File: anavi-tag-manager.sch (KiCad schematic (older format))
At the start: 26 parts, among them J1 USB_B_Micro, P1 CONN_01X03, SW1 SW_DIP_x01, U1 I2C_SENS_1, U2 I2C_SENS_1, U3 I2C_SENS_1, U4 Conn_01x04, U5 Conn_01x04, U6 Conn_01x04

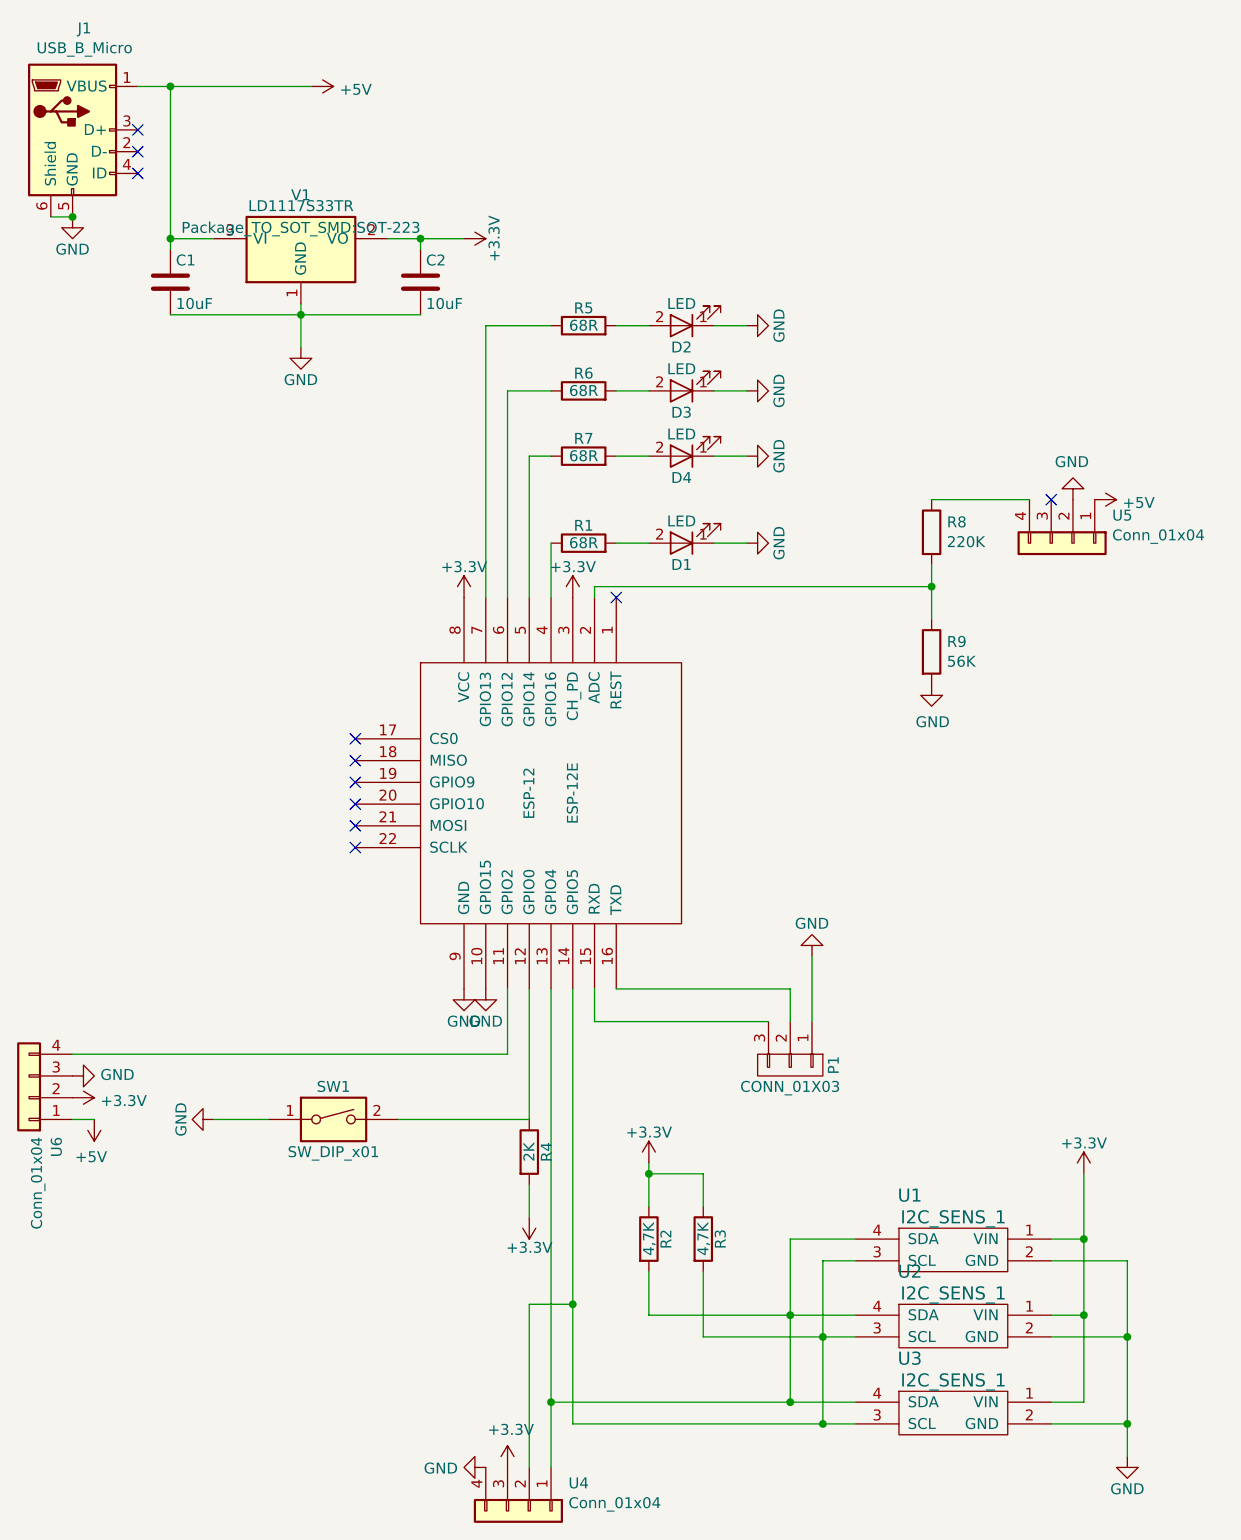
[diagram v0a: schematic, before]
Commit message: anavi-tag-manager.sch: Modify schematics
Remove unnecessary components inherited by ANAVI Gas Detector.
Add 4.7K resistor to GPIO15 of ESP8266. This way it is possible
to use this pin for SPI communicaiton after booting the board:
https://github.com/esp8266/Arduino/issues/2466#issuecomment-330794960

Signed-off-by: Leon Anavi <leon@anavi.org>
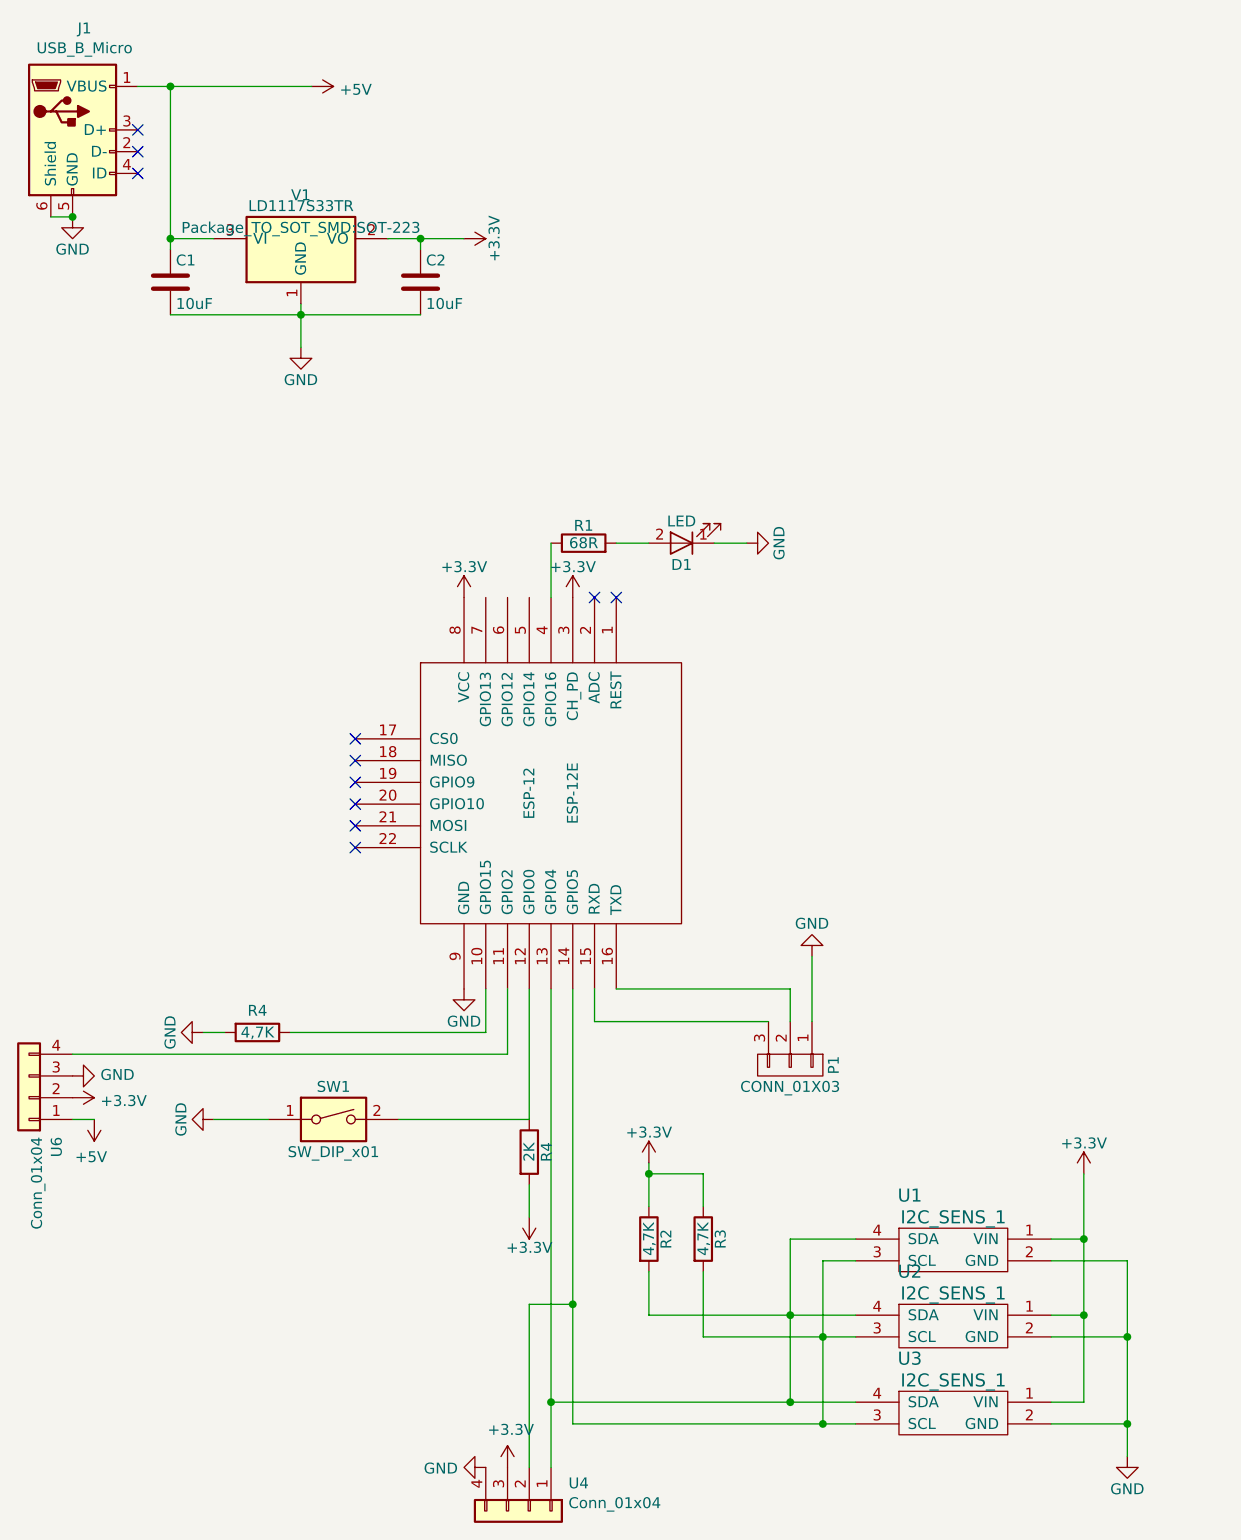
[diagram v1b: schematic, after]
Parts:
- removed D2, D3, D4: LED, LED_SMD:LED_1206_3216Metric, symbol anavi-tag-manager-rescue:LED-anavi-thermometer-rescue-anavi-gas-detector-rescue
- removed R5, R6, R7: 68R, Resistor_SMD:R_0603_1608Metric, symbol anavi-tag-manager-rescue:R-anavi-thermometer-rescue-anavi-gas-detector-rescue
- removed R8: 220K, Resistor_SMD:R_0603_1608Metric, symbol Device:R
- removed R9: 56K, Resistor_SMD:R_0603_1608Metric, symbol Device:R
- removed U5: Conn_01x04, Connector_PinHeader_2.54mm:PinHeader_1x04_P2.54mm_Vertical, symbol Connector_Generic:Conn_01x04
- added R4: 4,7K, Resistor_SMD:R_0603_1608Metric, symbol anavi-tag-manager-rescue:R-anavi-thermometer-rescue-anavi-gas-detector-rescue
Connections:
- net GND: now also R4.2; no longer ESP-12.10 (GPIO15)
- new net: ESP-12.10 (GPIO15), R4.1
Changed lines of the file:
@@
 L anavi-tag-manager-rescue:GND-anavi-thermometer-rescue-anavi-gas-detector-rescue #PWR018
 U 1 1 59B811E0
-P 2850 5100
-F 0 "#PWR018" H 2850 4850 50  0001 C CNN
-F 1 "GND" H 2850 4950 50  0000 C CNN
-F 2 "" H 2850 5100 50  0000 C CNN
-F 3 "" H 2850 5100 50  0000 C CNN
-	1    2850 5100
-	1    0    0    -1
+P 1550 5300
+F 0 "#PWR018" H 1550 5050 50  0001 C CNN
+F 1 "GND" H 1550 5150 50  0000 C CNN
+F 2 "" H 1550 5300 50  0000 C CNN
+F 3 "" H 1550 5300 50  0000 C CNN
+	1    1550 5300
+	0    1    1    0
 $EndComp
 $Comp
@@
 $EndComp
 $Comp
-L anavi-tag-manager-rescue:LED-anavi-thermometer-rescue-anavi-gas-detector-rescue D4
-U 1 1 5CAADB24
-P 3750 2650
-F 0 "D4" H 3750 2750 50  0000 C CNN
-F 1 "LED" H 3750 2550 50  0000 C CNN
-F 2 "LED_SMD:LED_1206_3216Metric" H 3750 2650 50  0001 C CNN
-F 3 "" H 3750 2650 50  0000 C CNN
-	1    3750 2650
-	-1   0    0    1
-$EndComp
-$Comp
-L anavi-tag-manager-rescue:R-anavi-thermometer-rescue-anavi-gas-detector-rescue R7
-U 1 1 5CAADB2B
-P 3300 2650
-F 0 "R7" V 3380 2650 50  0000 C CNN
-F 1 "68R" V 3300 2650 50  0000 C CNN
-F 2 "Resistor_SMD:R_0603_1608Metric" V 3230 2650 50  0001 C CNN
-F 3 "" H 3300 2650 50  0000 C CNN
-	1    3300 2650
-	0    -1   -1   0
-$EndComp
-$Comp
-L anavi-tag-manager-rescue:GND-anavi-thermometer-rescue-anavi-gas-detector-rescue #PWR?
-U 1 1 5CAADB32
-P 4050 2650
-F 0 "#PWR?" H 4050 2400 50  0001 C CNN
-F 1 "GND" H 4050 2500 50  0000 C CNN
-F 2 "" H 4050 2650 50  0000 C CNN
-F 3 "" H 4050 2650 50  0000 C CNN
-	1    4050 2650
-	0    -1   -1   0
-$EndComp
-Wire Wire Line
-	3450 2650 3600 2650
-Wire Wire Line
-	3900 2650 4050 2650
-$Comp
-L anavi-tag-manager-rescue:LED-anavi-thermometer-rescue-anavi-gas-detector-rescue D3
-U 1 1 5CAAEF49
-P 3750 2350
-F 0 "D3" H 3750 2450 50  0000 C CNN
-F 1 "LED" H 3750 2250 50  0000 C CNN
-F 2 "LED_SMD:LED_1206_3216Metric" H 3750 2350 50  0001 C CNN
-F 3 "" H 3750 2350 50  0000 C CNN
-	1    3750 2350
-	-1   0    0    1
-$EndComp
-$Comp
-L anavi-tag-manager-rescue:R-anavi-thermometer-rescue-anavi-gas-detector-rescue R6
-U 1 1 5CAAEF50
-P 3300 2350
-F 0 "R6" V 3380 2350 50  0000 C CNN
-F 1 "68R" V 3300 2350 50  0000 C CNN
-F 2 "Resistor_SMD:R_0603_1608Metric" V 3230 2350 50  0001 C CNN
-F 3 "" H 3300 2350 50  0000 C CNN
-	1    3300 2350
-	0    -1   -1   0
-$EndComp
-$Comp
-L anavi-tag-manager-rescue:GND-anavi-thermometer-rescue-anavi-gas-detector-rescue #PWR?
-U 1 1 5CAAEF57
-P 4050 2350
-F 0 "#PWR?" H 4050 2100 50  0001 C CNN
-F 1 "GND" H 4050 2200 50  0000 C CNN
-F 2 "" H 4050 2350 50  0000 C CNN
-F 3 "" H 4050 2350 50  0000 C CNN
-	1    4050 2350
-	0    -1   -1   0
-$EndComp
-Wire Wire Line
-	3450 2350 3600 2350
-Wire Wire Line
-	3900 2350 4050 2350
-$Comp
-L anavi-tag-manager-rescue:LED-anavi-thermometer-rescue-anavi-gas-detector-rescue D2
-U 1 1 5CAB04B0
-P 3750 2050
-F 0 "D2" H 3750 2150 50  0000 C CNN
-F 1 "LED" H 3750 1950 50  0000 C CNN
-F 2 "LED_SMD:LED_1206_3216Metric" H 3750 2050 50  0001 C CNN
-F 3 "" H 3750 2050 50  0000 C CNN
-	1    3750 2050
-	-1   0    0    1
-$EndComp
-$Comp
-L anavi-tag-manager-rescue:R-anavi-thermometer-rescue-anavi-gas-detector-rescue R5
-U 1 1 5CAB04B7
-P 3300 2050
-F 0 "R5" V 3380 2050 50  0000 C CNN
-F 1 "68R" V 3300 2050 50  0000 C CNN
-F 2 "Resistor_SMD:R_0603_1608Metric" V 3230 2050 50  0001 C CNN
-F 3 "" H 3300 2050 50  0000 C CNN
-	1    3300 2050
-	0    -1   -1   0
-$EndComp
-$Comp
-L anavi-tag-manager-rescue:GND-anavi-thermometer-rescue-anavi-gas-detector-rescue #PWR?
-U 1 1 5CAB04BE
-P 4050 2050
-F 0 "#PWR?" H 4050 1800 50  0001 C CNN
-F 1 "GND" H 4050 1900 50  0000 C CNN
-F 2 "" H 4050 2050 50  0000 C CNN
-F 3 "" H 4050 2050 50  0000 C CNN
-	1    4050 2050
-	0    -1   -1   0
-$EndComp
-Wire Wire Line
-	3450 2050 3600 2050
-Wire Wire Line
-	3900 2050 4050 2050
-Wire Wire Line
-	3050 3300 3050 2650
-Wire Wire Line
-	3050 2650 3150 2650
-Wire Wire Line
-	2950 3300 2950 2350
-Wire Wire Line
-	2950 2350 3150 2350
-Wire Wire Line
-	2850 3300 2850 2050
-Wire Wire Line
-	2850 2050 3150 2050
-$Comp
-L Connector_Generic:Conn_01x04 U5
-U 1 1 5CAB7080
-P 5550 3050
-F 0 "U5" V 5423 3230 50  0000 L CNN
-F 1 "Conn_01x04" V 5514 3230 50  0000 L CNN
-F 2 "Connector_PinHeader_2.54mm:PinHeader_1x04_P2.54mm_Vertical" H 5550 3050 50  0001 C CNN
-F 3 "~" H 5550 3050 50  0001 C CNN
-	1    5550 3050
-	0    1    1    0
-$EndComp
-Wire Wire Line
-	3350 3300 3350 3250
-$Comp
-L power:+5V #PWR?
-U 1 1 5CABC645
-P 5650 2850
-F 0 "#PWR?" H 5650 2700 50  0001 C CNN
-F 1 "+5V" V 5665 2978 50  0000 L CNN
-F 2 "" H 5650 2850 50  0001 C CNN
-F 3 "" H 5650 2850 50  0001 C CNN
-	1    5650 2850
-	0    1    1    0
-$EndComp
-$Comp
 L Connector_Generic:Conn_01x04 U6
 U 1 1 5CABCF1E
@@
 	0    1    1    0
 $EndComp
-NoConn ~ 5450 2850
-$Comp
-L power:GND #PWR?
-U 1 1 5CAC01B2
-P 5550 2850
-F 0 "#PWR?" H 5550 2600 50  0001 C CNN
-F 1 "GND" H 5555 2677 50  0000 C CNN
-F 2 "" H 5550 2850 50  0001 C CNN
-F 3 "" H 5550 2850 50  0001 C CNN
-	1    5550 2850
-	-1   0    0    1
-$EndComp
-$Comp
-L Device:R R8
-U 1 1 5CB2C30F
-P 4900 3000
-F 0 "R8" H 4970 3046 50  0000 L CNN
-F 1 "220K" H 4970 2955 50  0000 L CNN
-F 2 "Resistor_SMD:R_0603_1608Metric" V 4830 3000 50  0001 C CNN
-F 3 "~" H 4900 3000 50  0001 C CNN
-	1    4900 3000
-	1    0    0    -1
-$EndComp
-$Comp
-L Device:R R9
-U 1 1 5CB2C3AE
-P 4900 3550
-F 0 "R9" H 4970 3596 50  0000 L CNN
-F 1 "56K" H 4970 3505 50  0000 L CNN
-F 2 "Resistor_SMD:R_0603_1608Metric" V 4830 3550 50  0001 C CNN
-F 3 "~" H 4900 3550 50  0001 C CNN
-	1    4900 3550
-	1    0    0    -1
-$EndComp
-Wire Wire Line
-	3350 3250 4900 3250
-Wire Wire Line
-	4900 3250 4900 3150
-$Comp
-L power:GND #PWR?
-U 1 1 5CB3046F
-P 4900 3700
-F 0 "#PWR?" H 4900 3450 50  0001 C CNN
-F 1 "GND" H 4905 3527 50  0000 C CNN
-F 2 "" H 4900 3700 50  0001 C CNN
-F 3 "" H 4900 3700 50  0001 C CNN
-	1    4900 3700
-	1    0    0    -1
-$EndComp
-Wire Wire Line
-	4900 2850 5350 2850
-Wire Wire Line
-	4900 3400 4900 3250
-Connection ~ 4900 3250
+$Comp
+L anavi-tag-manager-rescue:R-anavi-thermometer-rescue-anavi-gas-detector-rescue R4
+U 1 1 5E11289E
+P 1800 5300
+F 0 "R4" V 1700 5300 50  0000 C CNN
+F 1 "4,7K" V 1800 5300 50  0000 C CNN
+F 2 "Resistor_SMD:R_0603_1608Metric" V 1730 5300 50  0001 C CNN
+F 3 "" H 1800 5300 50  0000 C CNN
+	1    1800 5300
+	0    1    1    0
+$EndComp
+Wire Wire Line
+	1550 5300 1650 5300
+Wire Wire Line
+	1950 5300 2850 5300
+Wire Wire Line
+	2850 5300 2850 5100
+NoConn ~ 3350 3300
 $EndSCHEMATC

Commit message: anavi-tag-manager.sch: Add SPI connector
Add a connector with 6 pins for SPI.

Signed-off-by: Leon Anavi <leon@anavi.org>
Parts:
- added SPI1: Conn_01x06, symbol Connector_Generic:Conn_01x06
- renumbered R4 to R5
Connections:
- net +3V3: now also SPI1.5 (Pin_5)
- net GND: now also SPI1.6 (Pin_6)
- net at ESP-12.10 (GPIO15), R5.1: now also SPI1.4 (Pin_4)
- net at ESP-12.5 (GPIO14): now also SPI1.1 (Pin_1)
- net at ESP-12.6 (GPIO12): now also SPI1.2 (Pin_2)
- net at ESP-12.7 (GPIO13): now also SPI1.3 (Pin_3)
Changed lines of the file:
@@
 	2950 5400 2950 5100
 $Comp
-L power:+5V #PWR?
+L power:+5V #PWR0104
 U 1 1 5CAA86B6
 P 1050 5700
-F 0 "#PWR?" H 1050 5550 50  0001 C CNN
+F 0 "#PWR0104" H 1050 5550 50  0001 C CNN
 F 1 "+5V" H 1065 5873 50  0000 C CNN
 F 2 "" H 1050 5700 50  0001 C CNN
@@
 	950  5700 1050 5700
 $Comp
-L power:GND #PWR?
+L power:GND #PWR0105
 U 1 1 5CAB955C
 P 950 5500
-F 0 "#PWR?" H 950 5250 50  0001 C CNN
+F 0 "#PWR0105" H 950 5250 50  0001 C CNN
 F 1 "GND" V 955 5372 50  0000 R CNN
 F 2 "" H 950 5500 50  0001 C CNN
@@
 $EndComp
 $Comp
-L power:+3.3V #PWR?
+L power:+3.3V #PWR0106
 U 1 1 5CAB97A0
 P 950 5600
-F 0 "#PWR?" H 950 5450 50  0001 C CNN
+F 0 "#PWR0106" H 950 5450 50  0001 C CNN
 F 1 "+3.3V" V 965 5728 50  0000 L CNN
 F 2 "" H 950 5600 50  0001 C CNN
@@
 $EndComp
 $Comp
-L anavi-tag-manager-rescue:R-anavi-thermometer-rescue-anavi-gas-detector-rescue R4
+L anavi-tag-manager-rescue:R-anavi-thermometer-rescue-anavi-gas-detector-rescue R5
 U 1 1 5E11289E
 P 1800 5300
-F 0 "R4" V 1700 5300 50  0000 C CNN
+F 0 "R5" V 1700 5300 50  0000 C CNN
 F 1 "4,7K" V 1800 5300 50  0000 C CNN
 F 2 "Resistor_SMD:R_0603_1608Metric" V 1730 5300 50  0001 C CNN
@@
 	2850 5300 2850 5100
 NoConn ~ 3350 3300
+$Comp
+L Connector_Generic:Conn_01x06 SPI1
+U 1 1 5E122C25
+P 2850 2150
+F 0 "SPI1" V 2816 1762 50  0000 R CNN
+F 1 "Conn_01x06" V 2725 1762 50  0000 R CNN
+F 2 "" H 2850 2150 50  0001 C CNN
+F 3 "~" H 2850 2150 50  0001 C CNN
+	1    2850 2150
+	0    -1   -1   0
+$EndComp
+$Comp
+L power:GND #PWR0107
+U 1 1 5E122EB7
+P 3150 2550
+F 0 "#PWR0107" H 3150 2300 50  0001 C CNN
+F 1 "GND" H 3155 2377 50  0000 C CNN
+F 2 "" H 3150 2550 50  0001 C CNN
+F 3 "" H 3150 2550 50  0001 C CNN
+	1    3150 2550
+	1    0    0    -1
+$EndComp
+$Comp
+L power:+3.3V #PWR0108
+U 1 1 5E122F58
+P 3050 2350
+F 0 "#PWR0108" H 3050 2200 50  0001 C CNN
+F 1 "+3.3V" H 3065 2523 50  0000 C CNN
+F 2 "" H 3050 2350 50  0001 C CNN
+F 3 "" H 3050 2350 50  0001 C CNN
+	1    3050 2350
+	-1   0    0    1
+$EndComp
+Wire Wire Line
+	3150 2550 3150 2350
+Wire Wire Line
+	2850 3300 2850 2350
+Wire Wire Line
+	2750 2350 2750 3000
+Wire Wire Line
+	2750 3000 2950 3000
+Wire Wire Line
+	2950 3000 2950 3300
+Wire Wire Line
+	2650 2350 2650 2800
+Wire Wire Line
+	2650 2800 3050 2800
+Wire Wire Line
+	3050 2800 3050 3300
+Connection ~ 1950 5300
+Wire Wire Line
+	1950 5300 1950 2450
+Wire Wire Line
+	1950 2450 2950 2450
+Wire Wire Line
+	2950 2450 2950 2350
 $EndSCHEMATC

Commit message: anavi-tag-manager.sch: Add 3.3V & assign footprints
Add an alternative 3.3V input for power supply from batteries.
Assign footprints to components.

Signed-off-by: Leon Anavi <leon@anavi.org>
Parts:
- added J2: Conn_01x02, Pin_Headers:Pin_Header_Straight_1x02, symbol Connector_Generic:Conn_01x02
- SPI1: footprint (none) -> Connector_PinHeader_2.54mm:PinHeader_1x06_P2.54mm_Vertical
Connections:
- net +3V3: now also J2.1 (Pin_1)
- net GND: now also J2.2 (Pin_2)
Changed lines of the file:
@@
 F 0 "SPI1" V 2816 1762 50  0000 R CNN
 F 1 "Conn_01x06" V 2725 1762 50  0000 R CNN
-F 2 "" H 2850 2150 50  0001 C CNN
+F 2 "Connector_PinHeader_2.54mm:PinHeader_1x06_P2.54mm_Vertical" H 2850 2150 50  0001 C CNN
 F 3 "~" H 2850 2150 50  0001 C CNN
 	1    2850 2150
@@
 Wire Wire Line
 	2950 2450 2950 2350
+$Comp
+L Connector_Generic:Conn_01x02 J2
+U 1 1 5E1230CA
+P 2750 950
+F 0 "J2" V 2716 762 50  0000 R CNN
+F 1 "Conn_01x02" V 2625 762 50  0000 R CNN
+F 2 "Pin_Headers:Pin_Header_Straight_1x02" H 2750 950 50  0001 C CNN
+F 3 "~" H 2750 950 50  0001 C CNN
+	1    2750 950
+	0    -1   -1   0
+$EndComp
+$Comp
+L power:GND #PWR0109
+U 1 1 5E125232
+P 2850 1150
+F 0 "#PWR0109" H 2850 900 50  0001 C CNN
+F 1 "GND" H 2855 977 50  0000 C CNN
+F 2 "" H 2850 1150 50  0001 C CNN
+F 3 "" H 2850 1150 50  0001 C CNN
+	1    2850 1150
+	1    0    0    -1
+$EndComp
+Wire Wire Line
+	2750 1650 2750 1150
+Connection ~ 2750 1650
 $EndSCHEMATC

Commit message: anavi-tag-manager.kicad_pcb: PCB routing
Apart from the routing, also change the position of GND on the
GPIO header (with IO2). The new order makes connecting servo
motors easier because the yellow wire should go to IO2, red wire
to 5V and black wire to GND.

Signed-off-by: Leon Anavi <leon@anavi.org>
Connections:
- net +3V3: now also U6.1 (Pin_1); no longer U6.2 (Pin_2)
- net +5V: now also U6.3 (Pin_3); no longer U6.1 (Pin_1)
- net GND: now also U6.2 (Pin_2); no longer U6.3 (Pin_3)
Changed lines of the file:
@@
 L power:+5V #PWR0104
 U 1 1 5CAA86B6
-P 1050 5700
-F 0 "#PWR0104" H 1050 5550 50  0001 C CNN
-F 1 "+5V" H 1065 5873 50  0000 C CNN
-F 2 "" H 1050 5700 50  0001 C CNN
-F 3 "" H 1050 5700 50  0001 C CNN
-	1    1050 5700
-	-1   0    0    1
+P 1150 5500
+F 0 "#PWR0104" H 1150 5350 50  0001 C CNN
+F 1 "+5V" H 1165 5673 50  0000 C CNN
+F 2 "" H 1150 5500 50  0001 C CNN
+F 3 "" H 1150 5500 50  0001 C CNN
+	1    1150 5500
+	0    1    1    0
 $EndComp
-Wire Wire Line
-	950  5700 1050 5700
 $Comp
 L power:GND #PWR0105
 U 1 1 5CAB955C
-P 950 5500
-F 0 "#PWR0105" H 950 5250 50  0001 C CNN
-F 1 "GND" V 955 5372 50  0000 R CNN
-F 2 "" H 950 5500 50  0001 C CNN
-F 3 "" H 950 5500 50  0001 C CNN
-	1    950  5500
+P 950 5600
+F 0 "#PWR0105" H 950 5350 50  0001 C CNN
+F 1 "GND" V 955 5472 50  0000 R CNN
+F 2 "" H 950 5600 50  0001 C CNN
+F 3 "" H 950 5600 50  0001 C CNN
+	1    950  5600
 	0    -1   -1   0
 $EndComp
@@
 L power:+3.3V #PWR0106
 U 1 1 5CAB97A0
-P 950 5600
-F 0 "#PWR0106" H 950 5450 50  0001 C CNN
-F 1 "+3.3V" V 965 5728 50  0000 L CNN
-F 2 "" H 950 5600 50  0001 C CNN
-F 3 "" H 950 5600 50  0001 C CNN
-	1    950  5600
+P 950 5700
+F 0 "#PWR0106" H 950 5550 50  0001 C CNN
+F 1 "+3.3V" V 965 5828 50  0000 L CNN
+F 2 "" H 950 5700 50  0001 C CNN
+F 3 "" H 950 5700 50  0001 C CNN
+	1    950  5700
 	0    1    1    0
 $EndComp
@@
 	2750 1650 2750 1150
 Connection ~ 2750 1650
+Wire Wire Line
+	950  5500 1150 5500
 $EndSCHEMATC
